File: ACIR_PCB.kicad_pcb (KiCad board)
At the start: 2 copper layers, 297 x 210 mm, 34 parts, among them J1 TestPoint, J10 TestPoint, J11 TestPoint, J12 TestPoint, J13 TestPoint, J14 TestPoint, J15 TestPoint, J2 TestPoint, J3 TestPoint, J4 TestPoint, J5 TestPoint, J6 TestPoint, J7 TestPoint, J8 TestPoint, J9 TestPoint

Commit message: Align 1S 4P test points horizontally, add Cell 4 test points (J16, J17), and connect pack test points
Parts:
- added J16: TestPoint, TestPoint:TestPoint_Bridge_Pitch2.54mm_Drill1.3mm, F.Cu at (175.0, 210.5)
- added J17: TestPoint, TestPoint:TestPoint_Bridge_Pitch2.54mm_Drill1.3mm, F.Cu at (78.0, 210.5)
- moved J10 1.27 mm to (175.0, 139.3), turned to 0 degrees
- moved J11 1.27 mm to (78.0, 139.3), turned to 0 degrees
- moved J12 1.27 mm to (175.0, 163.0), turned to 0 degrees
- moved J13 1.27 mm to (78.0, 163.0), turned to 0 degrees
- moved J14 1.27 mm to (175.0, 186.8), turned to 0 degrees
- moved J15 1.27 mm to (78.0, 186.8), turned to 0 degrees
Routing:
- net /4P_B+: track 471.0 -> 465.9 mm
- net /4P_B-: track 466.7 -> 462.9 mm
- net /4S_B-: track 77.0 -> 80.3 mm
- net /4S_B+: track 77.0 -> 80.3 mm

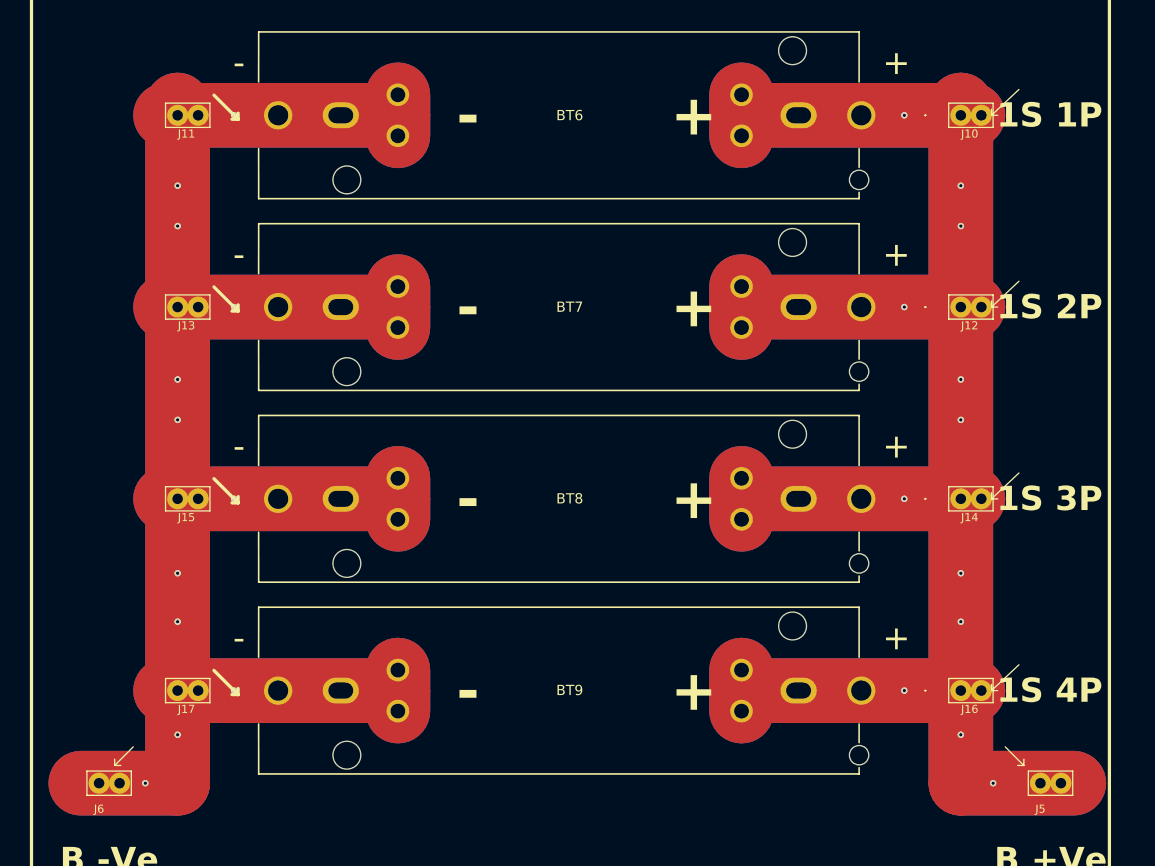
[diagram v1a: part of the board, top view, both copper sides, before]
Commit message: Update 1S 4P: 90-degree test points, exact symmetry, circular bare-copper zone with F.Mask aperture, and dense via stitching
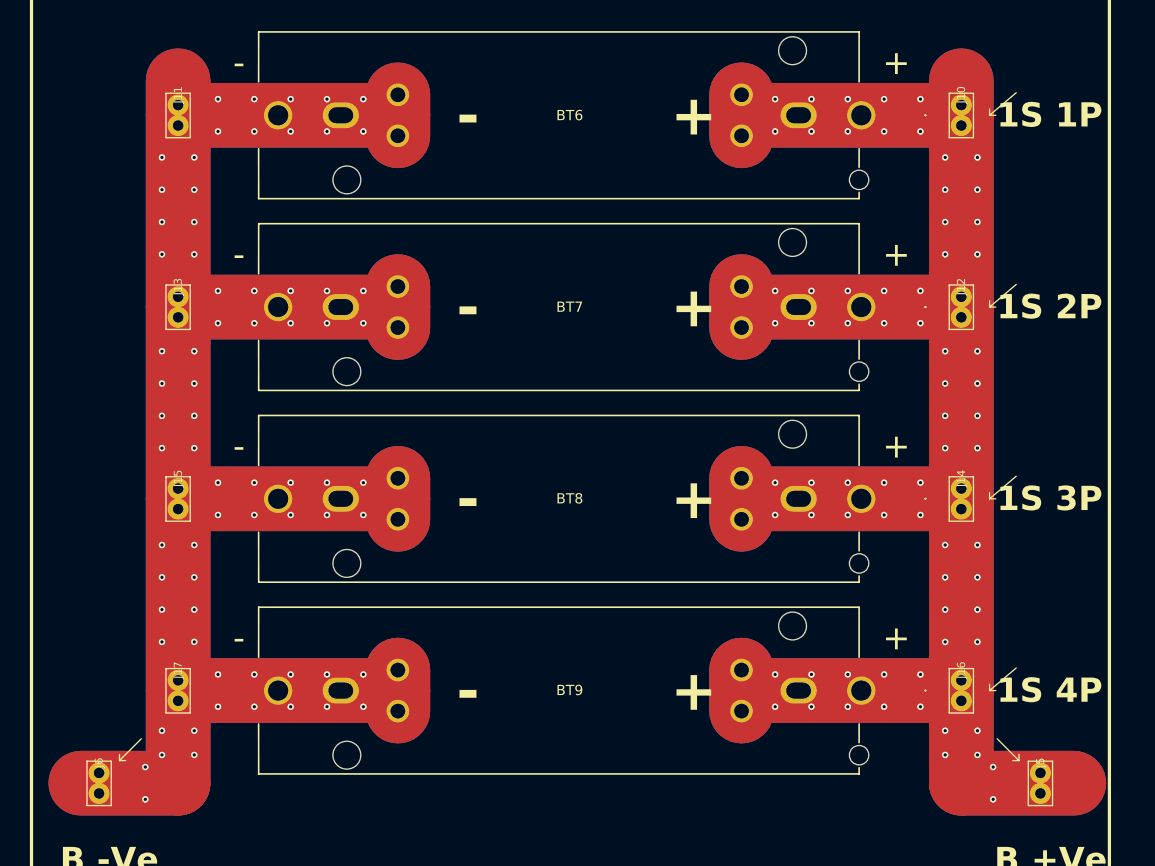
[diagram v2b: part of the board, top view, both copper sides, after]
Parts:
- moved J10 1.27 mm to (175.1, 140.6), turned to 90 degrees
- moved J11 1.27 mm to (78.1, 140.6), turned to 90 degrees
- moved J12 1.27 mm to (175.1, 164.3), turned to 90 degrees
- moved J13 1.27 mm to (78.1, 164.3), turned to 90 degrees
- moved J14 1.27 mm to (175.1, 188.1), turned to 90 degrees
- moved J15 1.27 mm to (78.1, 188.1), turned to 90 degrees
- moved J16 1.27 mm to (175.1, 211.8), turned to 90 degrees
- moved J17 1.27 mm to (78.1, 211.8), turned to 90 degrees
- moved J5 1.27 mm to (184.9, 223.3), turned to 90 degrees
- moved J6 1.27 mm to (68.3, 223.3), turned to 90 degrees
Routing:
- net /4P_B-: track 462.9 -> 456.5 mm, vias 16 -> 70
- net /4P_B+: track 465.9 -> 460.3 mm, vias 16 -> 70

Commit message: Align test points symmetrically, increase via stitching density, and update 4S1P and 1S1P modules
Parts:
- moved J7 2.55 mm to (216.0, 152.4)
- moved J8 2.55 mm to (320.4, 176.2)
- moved J9 2.55 mm to (216.0, 199.9)
- moved J3 2.54 mm to (320.4, 140.6)
- moved J4 2.54 mm to (320.4, 211.8)
- moved J1 2.52 mm to (248.0, 88.5)
- moved J2 2.52 mm to (146.8, 88.5)
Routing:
- net /4S_B-: track 80.3 -> 72.0 mm, vias 2 -> 18
- net /4S_B+: track 80.3 -> 72.0 mm, vias 2 -> 18
- net /1S_B-: track 73.9 -> 68.9 mm, vias 2 -> 18
- net /1S_B+: track 73.9 -> 68.9 mm, vias 2 -> 18
- net Net-(BT4--): track 190.6 -> 191.4 mm, vias 6 -> 40
- net Net-(BT3--): track 190.6 -> 191.4 mm, vias 6 -> 40
- net Net-(BT2--): track 190.6 -> 191.4 mm, vias 6 -> 40
- net /4P_B-: vias 70 -> 104
- net /4P_B+: vias 70 -> 104

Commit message: Make PCB production ready: clear silkscreen on copper, add comprehensive test point labels and arrows, and resolve all DRC warnings
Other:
- board text added: "1S 1P (+)"
- board text added: "1S 1P (-)"
- board text added: "1S 2P (+)"
- board text added: "1S 2P (-)"
- board text added: "1S 3P (+)"
- board text added: "1S 3P (-)"
- board text added: "1S 4P (+)"
- board text added: "1S 4P (-)"
- board text removed: "1S 2P"
- board text removed: "1S 3P"
- board text removed: "1S 4P"

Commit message: Update probing points with knockout badges, PT Sans font, and cell-by-cell +ve/-ve naming
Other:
- board text added: "1S 1P +ve"
- board text added: "1S 1P -ve"
- board text added: "1S 2P +ve"
- board text added: "1S 2P -ve"
- board text added: "1S 3P +ve"
- board text added: "1S 3P -ve"
- board text added: "1S 4P"
- board text added: "1S 4P +ve"
- board text added: "1S 4P -ve"
- board text added: "2S 1P +ve"
- board text added: "2S 1P -ve"
- board text added: "3S 1P +ve"
- board text added: "3S 1P -ve"
- board text added: "4S 1P +ve"
- board text added: "4S 1P -ve"
- board text added: "B +ve"
- board text added: "B -ve"
- board text removed: "1S 1P (+)"
- board text removed: "1S 1P (-)"
- board text removed: "1S 2P (+)"
- board text removed: "1S 2P (-)"
- board text removed: "1S 3P (+)"
- board text removed: "1S 3P (-)"
- board text removed: "1S 4P (+)"
- board text removed: "1S 4P (-)"
- board text removed: "2S 1P"
- board text removed: "3S 1P"
- board text removed: "B +Ve"
- board text removed: "B -Ve"

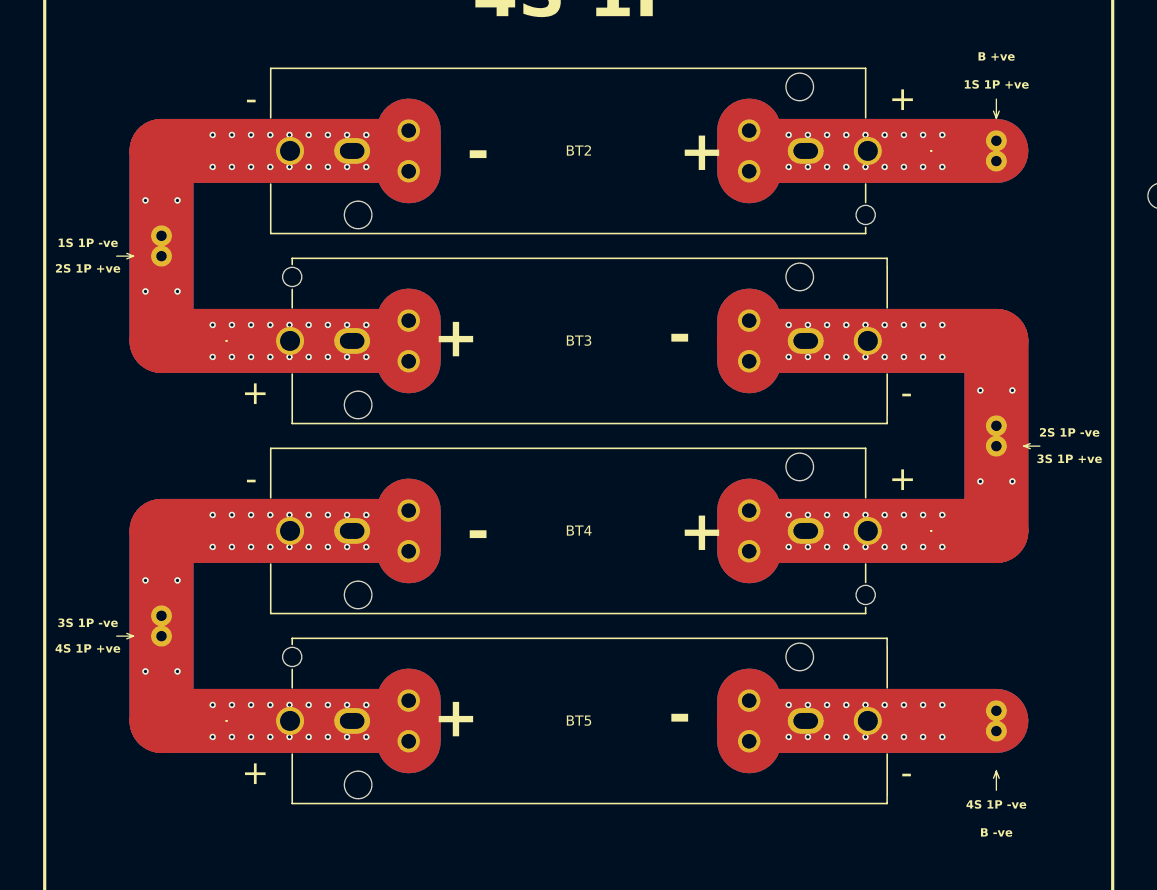
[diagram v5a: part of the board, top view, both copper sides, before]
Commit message: Add and align dedicated test points and bare-copper circular zones for every cell in 4S1P with knockout PT Sans labels
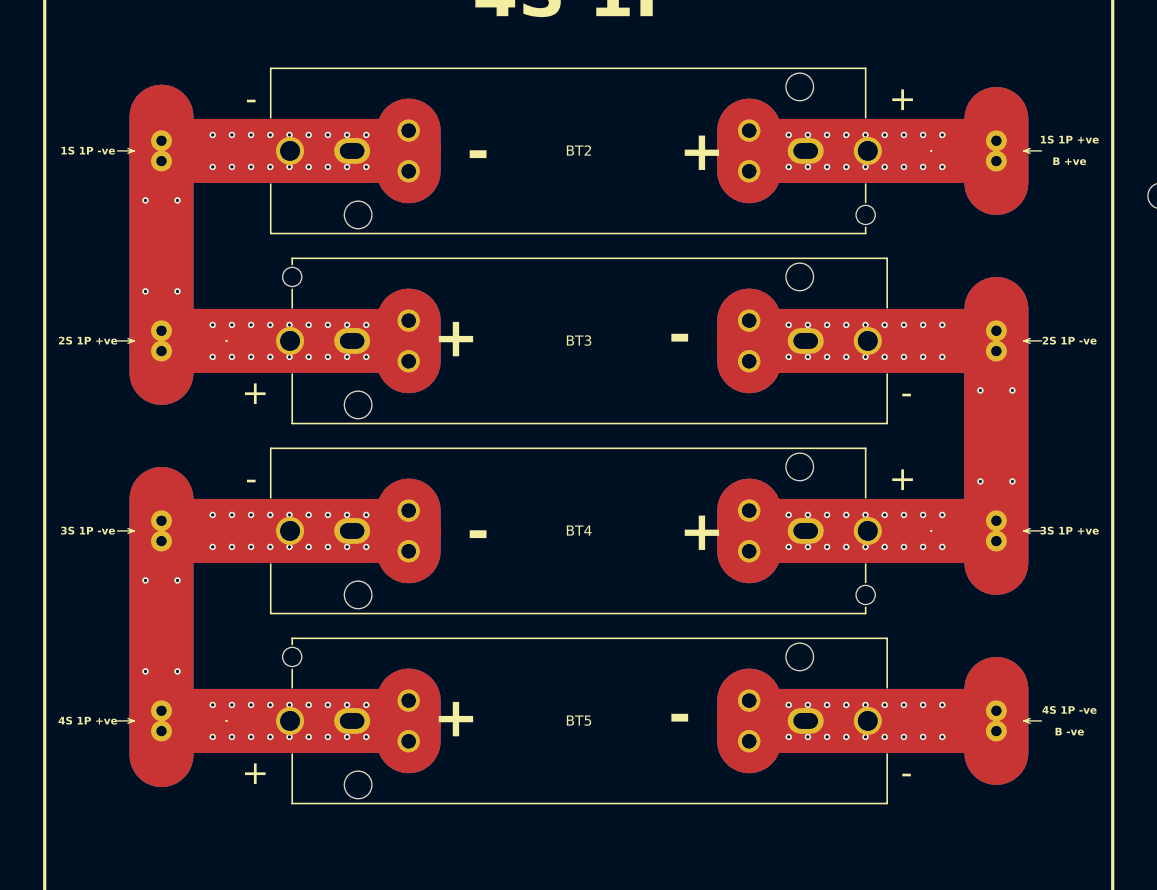
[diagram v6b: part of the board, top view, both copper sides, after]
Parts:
- added J18: TestPoint, TestPoint:TestPoint_Bridge_Pitch2.54mm_Drill1.3mm, F.Cu at (216.0, 164.3)
- added J19: TestPoint, TestPoint:TestPoint_Bridge_Pitch2.54mm_Drill1.3mm, F.Cu at (320.4, 188.1)
- added J20: TestPoint, TestPoint:TestPoint_Bridge_Pitch2.54mm_Drill1.3mm, F.Cu at (216.0, 211.8)
- moved J7 11.9 mm to (216.0, 140.6)
- moved J8 11.9 mm to (320.4, 164.3)
- moved J9 11.9 mm to (216.0, 188.1)
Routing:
- net Net-(BT2--): track 191.4 -> 208.0 mm
- net Net-(BT4--): track 191.4 -> 208.0 mm
- net Net-(BT3--): track 191.4 -> 207.4 mm
- net /4S_B-: track 72.0 -> 88.0 mm
- net /4S_B+: track 72.0 -> 88.0 mm

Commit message: Upgrade via stitching to ultra-dense 6-column arrays across all power rails and interconnects (1,792 stitched vias)
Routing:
- net Net-(BT4--): vias 40 -> 196
- net Net-(BT3--): vias 40 -> 202
- net Net-(BT2--): vias 40 -> 196
- net /4S_B-: vias 18 -> 72
- net /4S_B+: vias 18 -> 72
- net /4P_B-: vias 104 -> 462
- net /4P_B+: vias 104 -> 470
- net /1S_B-: vias 18 -> 62
- net /1S_B+: vias 18 -> 60

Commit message: Enlarge test point labels and knockout badges across all modules for clear eye visibility (1.4mm to 1.6mm font)
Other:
- board text added: "+ve"
- board text added: "-ve"
- board text added: "2S 1P"
- board text added: "3S 1P"
- board text removed: "1S 4P"
- board text removed: "2S 1P +ve"
- board text removed: "2S 1P -ve"
- board text removed: "3S 1P +ve"
- board text removed: "3S 1P -ve"
- board text removed: "4S 1P +ve"
